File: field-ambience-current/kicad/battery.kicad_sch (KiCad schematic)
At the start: 22 parts, among them J9 JST PH 2.0 2-pin (LiPo Batter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, Q1 DMG2305UX P-MOS SOT-23 (USB-C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, U7 MCP73831T-2ACI/OT (LiPo Charg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, U8 TPS61089RNR (Boost LiPo→5V, 2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

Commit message: kicad(gen): flow the 5 sourcing-fix part swaps into the generator (r18.71)
The generator is the schematic's source of truth, so the BOM part swaps must
live here (previously only in BOM/HTML). Swapped LCSC + MPN in the generator,
regenerated the .kicad_sch, re-exported jlc_bom.csv:
- FB2 ferrite C84094 -> C19330 (same Murata MPN, JLC 950k)
- VCAP C24539 -> C23630 (2.2uF 16V X5R 0603, JLC Basic)
- charger LED C72041 (blue+EOL!) -> C965800 (orange 605nm 0603)
- C_BULK2 C2880380 (stock 1) -> C23742 (100uF 10V X5R 1210)
- modifier buttons SW6-10 C2845240 (stock 30) -> C36498965 (HX B3F square
  head); footprint SW_TC1212-7.3_THT_4P reused, HX pinout verify noted in FP_NOTE.

The generated schematic Aron opens now carries the correct in-stock parts.
check_pinmap passes; jlc_bom.csv has the new codes (old ones gone).

Co-Authored-By: Claude Opus 4.8 <noreply@anthropic.com>
Claude-Session: https://claude.ai/code/session_01K5kLTFpDCCoYwx2dq6RkAv
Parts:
- LED_CHRG: LCSC C72041 -> C965800; MPN Generic amber 0603 -> XL-1608UOC-06; Manufacturer (none) -> XINGLIGHT
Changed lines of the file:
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@@
       (property "Datasheet" "~" (at 67.0 74.92 0)
         (effects (font (size 1.27 1.27)) hide))
-      (property "MPN" "Generic amber 0603" (at 69.54 78.73 0)
+      (property "MPN" "XL-1608UOC-06" (at 69.54 78.73 0)
         (effects (font (size 1.27 1.27)) hide))
-      (property "LCSC" "C72041" (at 69.54 80.0 0)
+      (property "Manufacturer" "XINGLIGHT" (at 69.54 80.0 0)
+        (effects (font (size 1.27 1.27)) hide))
+      (property "LCSC" "C965800" (at 69.54 81.27 0)
         (effects (font (size 1.27 1.27)) hide))
     (instances

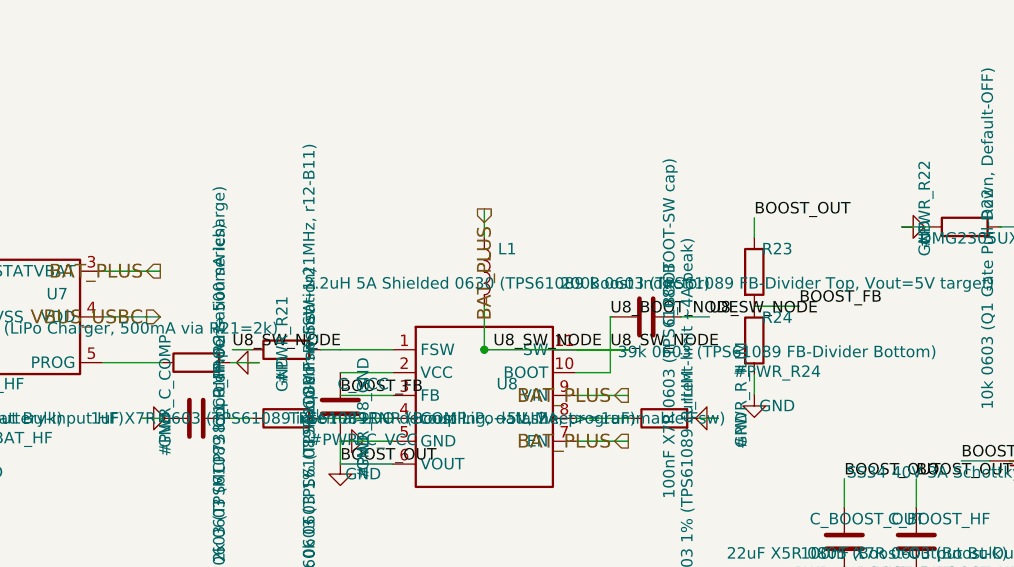
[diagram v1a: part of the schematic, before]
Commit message: fix(bom): L1 boost inductor had a dead LCSC link + nonexistent MPN (r18.77) (#89)
User reported: clicking L1 in Aron's BOM HTML (LCSC/JLC page link) led
nowhere -- the component doesn't exist on the site.

Root cause, verified two ways independently:

1. LCSC C83455 (the code in both the schematic and BOM_MASTER.md) 404s.
   It was never a valid listing, despite an r18.20c note in the changelog
   claiming it was "checked. Extended" -- that check apparently never
   actually loaded the live page. The r18.37 BOM<->generator string-diff
   audit couldn't catch this either, since both files carried the same
   wrong code -- a consistency check between two documents cannot detect
   an error that's identical in both.

2. The MPN itself, "SWPA6045S2R2MT", does not exist. Fetched Sunlord's own
   official SWPA6045S series datasheet (spec no. SWPA07160000) directly:
   its part-numbering table shows the "M" tolerance suffix (+-20%) is only
   used for inductance values >=4.3uH; every value below that, including
   2.2uH, only ships with the "N" suffix (+-30%). So "...S2R2MT" was
   never a real, orderable part number to begin with.

Verified the real part two independent ways: found LCSC C36500 via
JLCPCB's own catalog search, then cross-checked every electrical value
against Sunlord's official datasheet table (Item 12): 2.2uH, DCR 18mOhm
max, Isat 6.75A max / 7.40A typ, Irms 4.60A max / 5.00A typ -- an exact
match. Real part: SWPA6045S2R2NT, LCSC C36500, in stock.

Also found and fixed two related bugs surfaced during the investigation:
- The schematic's `value` field for L1 still described a completely
  different, older part: "Sumida CDR63B-2R2" in a "0630" case
  (6.0x3.0mm) -- a leftover from before the design switched to the
  Sunlord SWPA6045S (6.0x6.0x4.5mm). PCB_FOOTPRINT_RISK_AUDIT.md carried
  a fabricated "Isat 4.5A" figure that matched no datasheet row, and
  ADR-0011's enclosure Z-budget still listed the old 3.0mm Sumida height
  instead of the real 4.5mm (co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
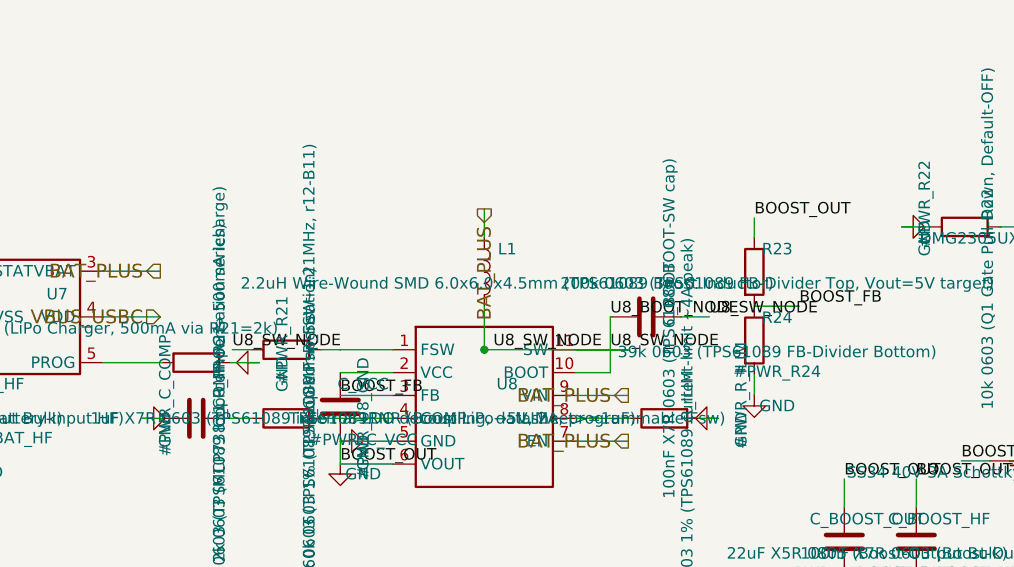
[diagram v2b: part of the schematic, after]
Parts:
- L1: value 2.2uH 5A Shielded 0630 (TPS61089 Boost Inductor) -> 2.2uH Wire-Wound SMD 6.0x6.0x4.5mm (TPS61089 Boost Inductor); FP_NOTE (none) -> r18.77: corrected from SWPA6045S2R2MT/C83455 (both wrong --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; LCSC C83455 -> C36500; MPN SWPA6045S2R2MT -> SWPA6045S2R2NT
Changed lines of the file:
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@@
       (property "Reference" "L1" (at 142.54 72.46 0)
         (effects (font (size 1.27 1.27))))
-      (property "Value" "2.2uH 5A Shielded 0630 (TPS61089 Boost Inductor)" (at 142.54 76.27 0)
+      (property "Value" "2.2uH Wire-Wound SMD 6.0x6.0x4.5mm (TPS61089 Boost Inductor)" (at 142.54 76.27 0)
         (effects (font (size 1.27 1.27))))
       (property "Footprint" "field_ambience:L_Sunlord_SWPA6045" (at 140 75 0)
@@
       (property "Datasheet" "~" (at 140 75 0)
         (effects (font (size 1.27 1.27)) hide))
-      (property "MPN" "SWPA6045S2R2MT" (at 142.54 78.81 0)
+      (property "MPN" "SWPA6045S2R2NT" (at 142.54 78.81 0)
         (effects (font (size 1.27 1.27)) hide))
-      (property "LCSC" "C83455" (at 142.54 80.08 0)
+      (property "LCSC" "C36500" (at 142.54 80.08 0)
+        (effects (font (size 1.27 1.27)) hide))
+      (property "FP_NOTE" "r18.77: corrected from SWPA6045S2R2MT/C83455 (both wrong -- MT suffix does not exist for 2.2uH per Sunlord's own datasheet, only NT; C83455 was a dead LCSC listing). Verified against Sunlord's official SWPA6045S series datasheet (Item 12 table): 2.2uH, DCR 18mOhm max, Isat 7.40A typ, Irms 5.00A typ, tolerance N=+-30%. LCSC C36500 cross-checked live via JLCPCB catalog." (at 142.54 81.35 0)
         (effects (font (size 1.27 1.27)) hide))
     (instances
